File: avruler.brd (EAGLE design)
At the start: 152.9 x 20.3 mm, 15 parts, among them IC1 TINY45, IC3 TINY45

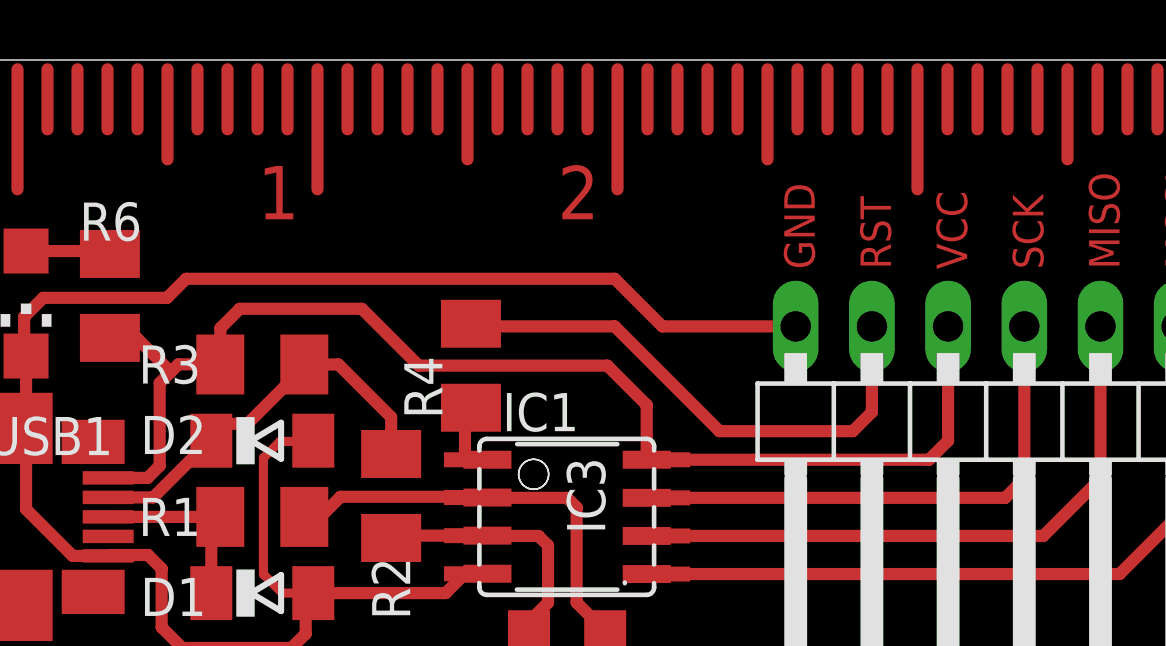
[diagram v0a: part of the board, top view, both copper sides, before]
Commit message: swapped VCC and RESET on the pinheader
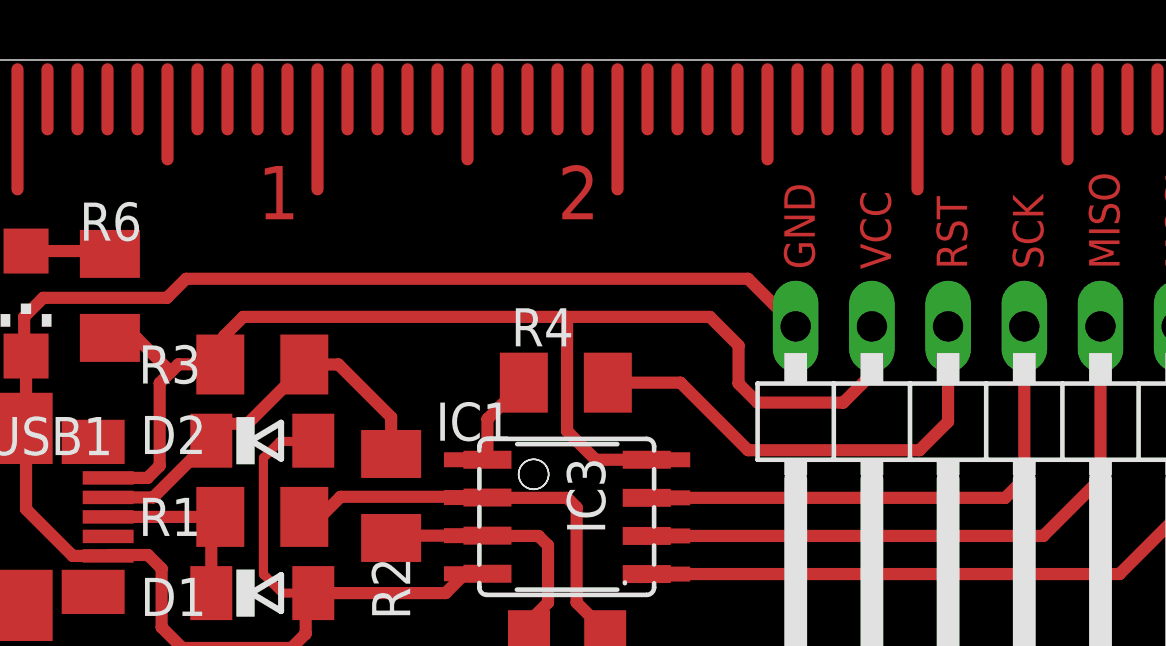
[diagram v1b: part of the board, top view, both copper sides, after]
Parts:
- moved R4 3.21 mm to (20.3, 9.55), turned to 180 degrees
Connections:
- net N$10: now also JP1.4; no longer JP1.5
- net VCC: now also JP1.5; no longer JP1.4
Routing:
- net N$10: track 18.0 -> 15.8 mm
- net VCC: track 42.4 -> 43.8 mm
- net N$1: track 2.57 -> 3.82 mm
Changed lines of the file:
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@@
 <setting verticaltext="up"/>
 </settings>
-<grid distance="50" unitdist="mil" unit="mil" style="lines" multiple="1" display="no" altdistance="0.025" altunitdist="inch" altunit="inch"/>
+<grid distance="12.5" unitdist="mil" unit="mil" style="lines" multiple="1" display="no" altdistance="0.025" altunitdist="inch" altunit="inch"/>
 <layers>
 <layer number="1" name="Top" color="4" fill="1" visible="yes" active="yes"/>
@@
 <text x="148.5" y="15" size="1.778" layer="1">15</text>
 <text x="28.575" y="13.335" size="1.016" layer="1" rot="R90">GND</text>
-<text x="31.115" y="13.335" size="1.016" layer="1" rot="R90">RST</text>
-<text x="33.655" y="13.335" size="1.016" layer="1" rot="R90">VCC</text>
+<text x="33.655" y="13.335" size="1.016" layer="1" rot="R90">RST</text>
+<text x="31.115" y="13.335" size="1.016" layer="1" rot="R90">VCC</text>
 <text x="36.195" y="13.335" size="1.016" layer="1" rot="R90">SCK</text>
 <text x="38.735" y="13.335" size="1.016" layer="1" rot="R90">MISO</text>
@@
 <attribute name="MF" value="" x="16.51" y="-12.7" size="1.778" layer="27" rot="R270" display="off"/>
 <attribute name="OC_FARNELL" value="1455133" x="16.51" y="-12.7" size="1.778" layer="27" rot="R270" display="off"/>
-<attribute name="NAME" x="18.161" y="7.9375" size="1.27" layer="25" ratio="10"/>
+<attribute name="NAME" x="15.9385" y="7.62" size="1.27" layer="25" ratio="10"/>
 <attribute name="VALUE" x="21.336" y="0.6985" size="1.27" layer="27" ratio="10"/>
 </element>
@@
 <attribute name="VALUE" x="24.765" y="11.43" size="1.27" layer="27" rot="R270"/>
 </element>
-<element name="R4" library="resistor" package="M1206" value="0" x="17.115215625" y="10.118034375" smashed="yes" rot="R270">
-<attribute name="NAME" x="14.892715625" y="10.435534375" size="1.27" layer="25" rot="R270"/>
-<attribute name="VALUE" x="18.385215625" y="12.023034375" size="1.27" layer="27" rot="R270"/>
+<element name="R4" library="resistor" package="M1206" value="0" x="20.278034375" y="9.554784375" smashed="yes" rot="R180">
+<attribute name="NAME" x="18.456965625" y="10.765215625" size="1.27" layer="25"/>
+<attribute name="VALUE" x="22.266965625" y="8.542715625" size="1.27" layer="27"/>
 </element>
 <element name="LED1" library="led" package="CHIPLED_1206" value="" x="2.286" y="12.192" smashed="yes" rot="R180">
@@
 <wire x1="16.916" y1="6.985" x2="17.666" y2="6.985" width="0.4064" layer="1"/>
 <contactref element="R4" pad="2"/>
-<wire x1="16.916" y1="6.985" x2="16.916" y2="8.51881875" width="0.4064" layer="1"/>
-<wire x1="16.916" y1="8.51881875" x2="17.115215625" y2="8.718034375" width="0.4064" layer="1"/>
+<wire x1="17.666" y1="6.985" x2="17.666" y2="8.34275" width="0.4064" layer="1"/>
+<wire x1="17.666" y1="8.34275" x2="18.878034375" y2="9.554784375" width="0.4064" layer="1"/>
 </signal>
 <signal name="N$2">
@@
 <wire x1="8.754221875" y1="10.165778125" x2="8.76" y2="10.16" width="0.4064" layer="1"/>
 <wire x1="22.974" y1="6.985" x2="23.724" y2="6.985" width="0.4064" layer="1"/>
-<wire x1="22.974" y1="6.985" x2="22.974" y2="8.810175" width="0.4064" layer="1"/>
-<wire x1="22.974" y1="8.810175" x2="21.66194375" y2="10.12223125" width="0.4064" layer="1"/>
-<wire x1="21.66194375" y1="10.12223125" x2="15.374725" y2="10.12223125" width="0.4064" layer="1"/>
-<wire x1="15.374725" y1="10.12223125" x2="13.4795" y2="12.01745625" width="0.4064" layer="1"/>
-<wire x1="13.4795" y1="12.01745625" x2="9.409928125" y2="12.01745625" width="0.4064" layer="1"/>
-<wire x1="9.409928125" y1="12.01745625" x2="8.763828125" y2="11.37135625" width="0.4064" layer="1"/>
-<wire x1="8.763828125" y1="11.37135625" x2="8.763828125" y2="10.163828125" width="0.4064" layer="1"/>
-<wire x1="8.763828125" y1="10.163828125" x2="8.76" y2="10.16" width="0.4064" layer="1"/>
 <contactref element="R6" pad="2"/>
 <wire x1="5.08" y1="11.046" x2="5.972003125" y2="11.046" width="0.4064" layer="1"/>
 <wire x1="5.972003125" y1="11.046" x2="7.1082125" y2="9.909790625" width="0.4064" layer="1"/>
-<contactref element="JP1" pad="4"/>
-<wire x1="23.724" y1="6.985" x2="32.385" y2="6.985" width="0.4064" layer="1"/>
-<wire x1="32.385" y1="6.985" x2="33.02" y2="7.62" width="0.4064" layer="1"/>
-<wire x1="33.02" y1="7.62" x2="33.02" y2="11.43" width="0.4064" layer="1"/>
+<contactref element="JP1" pad="5"/>
+<wire x1="22.974" y1="6.985" x2="21.2725" y2="6.985" width="0.4064" layer="1"/>
+<wire x1="21.2725" y1="6.985" x2="20.32" y2="7.9375" width="0.4064" layer="1"/>
+<wire x1="20.32" y1="7.9375" x2="20.32" y2="11.7475" width="0.4064" layer="1"/>
+<wire x1="20.32" y1="11.7475" x2="9.525" y2="11.7475" width="0.4064" layer="1"/>
+<wire x1="9.525" y1="11.7475" x2="8.89" y2="11.1125" width="0.4064" layer="1"/>
+<wire x1="8.89" y1="11.1125" x2="8.89" y2="10.29" width="0.4064" layer="1"/>
+<wire x1="8.89" y1="10.29" x2="8.76" y2="10.16" width="0.4064" layer="1"/>
+<wire x1="30.48" y1="11.43" x2="30.48" y2="9.8425" width="0.4064" layer="1"/>
+<wire x1="30.48" y1="9.8425" x2="29.5275" y2="8.89" width="0.4064" layer="1"/>
+<wire x1="29.5275" y1="8.89" x2="26.67" y2="8.89" width="0.4064" layer="1"/>
+<wire x1="26.67" y1="8.89" x2="26.035" y2="9.525" width="0.4064" layer="1"/>
+<wire x1="26.035" y1="9.525" x2="26.035" y2="10.795" width="0.4064" layer="1"/>
+<wire x1="26.035" y1="10.795" x2="25.0825" y2="11.7475" width="0.4064" layer="1"/>
+<wire x1="25.0825" y1="11.7475" x2="20.32" y2="11.7475" width="0.4064" layer="1"/>
 </signal>
 <signal name="GND">
@@
 <wire x1="5.0525" y1="3.81" x2="5.0225" y2="3.78" width="0.4064" layer="1"/>
 <contactref element="JP1" pad="6"/>
-<wire x1="27.94" y1="11.43" x2="23.495" y2="11.43" width="0.4064" layer="1"/>
-<wire x1="23.495" y1="11.43" x2="21.9075" y2="13.0175" width="0.4064" layer="1"/>
-<wire x1="21.9075" y1="13.0175" x2="7.62" y2="13.0175" width="0.4064" layer="1"/>
+<wire x1="27.94" y1="11.43" x2="26.3525" y2="13.0175" width="0.4064" layer="1"/>
+<wire x1="26.3525" y1="13.0175" x2="7.62" y2="13.0175" width="0.4064" layer="1"/>
 <wire x1="7.62" y1="13.0175" x2="6.985" y2="12.3825" width="0.4064" layer="1"/>
 <wire x1="6.985" y1="12.3825" x2="2.8575" y2="12.3825" width="0.4064" layer="1"/>
@@
 <wire x1="4.984" y1="13.942" x2="5.08" y2="13.846" width="0.4064" layer="1"/>
 </signal>
-<signal name="N$10">
-<contactref element="R4" pad="1"/>
-<contactref element="JP1" pad="5"/>
-<wire x1="30.48" y1="11.43" x2="30.48" y2="8.5725" width="0.4064" layer="1"/>
-<wire x1="30.48" y1="8.5725" x2="29.845" y2="7.9375" width="0.4064" layer="1"/>
-<wire x1="29.845" y1="7.9375" x2="25.4" y2="7.9375" width="0.4064" layer="1"/>
-<wire x1="25.4" y1="7.9375" x2="21.9075" y2="11.43" width="0.4064" layer="1"/>
-<wire x1="21.9075" y1="11.43" x2="17.20325" y2="11.43" width="0.4064" layer="1"/>
-<wire x1="17.20325" y1="11.43" x2="17.115215625" y2="11.518034375" width="0.4064" layer="1"/>
-</signal>
 <signal name="N$9">
 <wire x1="143" y1="20" x2="143" y2="18" width="0.4064" layer="1"/>
@@
 <wire x1="139.7" y1="0" x2="139.7" y2="7.62" width="0.4064" layer="1"/>
 </signal>
+<signal name="N$10">
+<contactref element="JP1" pad="4"/>
+<contactref element="R4" pad="1"/>
+<wire x1="21.678034375" y1="9.554784375" x2="24.100215625" y2="9.554784375" width="0.4064" layer="1"/>
+<wire x1="24.100215625" y1="9.554784375" x2="26.3525" y2="7.3025" width="0.4064" layer="1"/>
+<wire x1="26.3525" y1="7.3025" x2="32.0675" y2="7.3025" width="0.4064" layer="1"/>
+<wire x1="32.0675" y1="7.3025" x2="33.02" y2="8.255" width="0.4064" layer="1"/>
+<wire x1="33.02" y1="8.255" x2="33.02" y2="11.43" width="0.4064" layer="1"/>
+</signal>
 </signals>
